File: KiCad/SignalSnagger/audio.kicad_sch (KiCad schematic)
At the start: 56 parts, among them U301 LM386, U302 LT6231, U303 LT6231, U304 LM386

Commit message: Ver 0.24
Schematic updates.
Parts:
- removed SW301: (no value), symbol Switch:SW_SPST
- added C326: 100nF, symbol Device:C_Small
- added C327: 1uF, symbol Device:C_Small
- added D302: CDBA340-HF, Diode_SMD:D_SMA, symbol Diode:CDBA340-HF
- added J302, J303, J304: 36-5006-ND, symbol Connector_Generic:Conn_01x01
- added JP301: (no value), symbol Jumper:SolderJumper_2_Open
- added R323: (no value), symbol Device:R_US
- added R324: 330k, symbol Device:R_US
- added R325: 10k, symbol Device:R_US
- added R326: 1k, symbol Device:R_US
- added R327: 51k, symbol Device:R_US
- J301: value (none) -> Headphones
- R316: value (none) -> 470
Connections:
- net +5V: now also R324.1
- net GND: now also C327.1, J304.1 (Pin_1), R325.2, R327.2
- net Headphone: now also C326.1, JP301.1 (A)
- net I OUT: now also J303.1 (Pin_1)
- net Q OUT: now also J302.1 (Pin_1)
- net at C308.1: now also R323.1
- net at J301.S: now also JP301.2 (B), R323.2
- new net: D302.1 (K), R326.1
- new net: C326.2, D302.2 (A), R324.2, R325.1
- new net ASSI_FAR: C327.2, R326.2, R327.1
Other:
- note removed: "How to protect U301 in the event that someone uses a mono headphone plug?"
- moved on the sheet: C301, C302, C303, C304, C305, C306, C307, C308, C309, C310, C311, C312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

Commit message: V0.25
Schematic updates
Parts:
- removed C312, C317: 100nF, symbol Device:C_Small
- JP301: value (none) -> SolderJumper_2_Open
- R323: value (none) -> 10
- U302, U303: value LT6231 -> TS912IDT; footprint Package_TO_SOT_SMD:TSOT-23-6 -> Package_SO:SO-8_3.9x4.9mm_P1.27mm
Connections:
- net +5V: no longer U302.8 (V+), U303.8 (V+)
- net GND: no longer U302.4 (V-), U303.4 (V-)
- net VG: now also U302.5 (+), U303.5 (+); no longer U302.3 (+), U303.3 (+)
- net at C316.1, C318.2, R319.2: now also U303.7 (OUT); no longer U303.1 (OUT)
- net at C315.1, R319.1: now also U303.6 (-); no longer U303.2 (-)
- net at C310.1, R306.1: now also U302.6 (-); no longer U302.2 (-)
- net at C309.1, C311.1, C313.1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: now also U302.7 (OUT); no longer U302.1 (OUT)
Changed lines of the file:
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@@
   (title_block
     (title "SignalSnagger")
-    (date "2024-02-03")
-    (rev "0.24")
+    (date "2024-02-09")
+    (rev "0.25")
   )
   (junction (at 30.48 160.02) (diameter 0) (color 0 0 0 0)
@@
   (junction (at 196.85 46.99) (diameter 0) (color 0 0 0 0)
   )
-  (junction (at 85.09 48.26) (diameter 0) (color 0 0 0 0)
-  )
   (junction (at 97.79 57.15) (diameter 0) (color 0 0 0 0)
   )
@@
   )
   (junction (at 106.68 151.13) (diameter 0) (color 0 0 0 0)
-  )
-  (junction (at 85.09 142.24) (diameter 0) (color 0 0 0 0)
   )
   (junction (at 238.76 127) (diameter 0) (color 0 0 0 0)
@@
     (stroke (width 0) (type default) (color 0 0 0 0))
   )
-  (wire (pts (xy 86.36 48.26) (xy 85.09 48.26))
-    (stroke (width 0) (type default) (color 0 0 0 0))
-  )
   (wire (pts (xy 72.39 54.61) (xy 76.2 54.61))
     (stroke (width 0) (type default) (color 0 0 0 0))
@@
     (stroke (width 0) (type default) (color 0 0 0 0))
   )
-  (wire (pts (xy 85.09 48.26) (xy 85.09 49.53))
-    (stroke (width 0) (type default) (color 0 0 0 0))
-  )
   (wire (pts (xy 196.85 69.85) (xy 196.85 67.31))
     (stroke (width 0) (type default) (color 0 0 0 0))
@@
     (stroke (width 0) (type default) (color 0 0 0 0))
   )
-  (wire (pts (xy 86.36 142.24) (xy 85.09 142.24))
-    (stroke (width 0) (type default) (color 0 0 0 0))
-  )
   (wire (pts (xy 196.85 107.95) (xy 199.39 107.95))
     (stroke (width 0) (type default) (color 0 0 0 0))
@@
   )
   (wire (pts (xy 124.46 152.4) (xy 124.46 151.13))
-    (stroke (width 0) (type default) (color 0 0 0 0))
-  )
-  (wire (pts (xy 85.09 142.24) (xy 85.09 143.51))
     (stroke (width 0) (type default) (color 0 0 0 0))
   )
@@
       (effects (font (size 1.27 1.27)) (justify left))
     )
-    (property "Value" "" (id 1) (at 227.711 79.1722 0)
+    (property "Value" "10" (id 1) (at 227.711 79.1722 0)
       (effects (font (size 1.27 1.27)) (justify left))
     )
@@
     (pin "3")
   )
-  (symbol (lib_id "Amplifier_Operational:LT6231") (at 87.63 57.15 0) (mirror x) (unit 1)
+  (symbol (lib_id "Amplifier_Operational:LT6231") (at 87.63 57.15 0) (mirror x) (unit 2)
     (in_bom yes) (on_board yes)
     (property "Reference" "U303" (id 0) (at 87.63 53.34 0)
       (effects (font (size 1.524 1.524) bold) (justify left))
     )
-    (property "Value" "LT6231" (id 1) (at 82.55 57.15 0)
-      (effects (font (size 1.27 1.27)) (justify left))
-    )
-    (property "Footprint" "Package_TO_SOT_SMD:TSOT-23-6" (id 2) (at 87.63 50.8 0)
+    (property "Value" "TS912IDT" (id 1) (at 82.55 57.15 0)
+      (effects (font (size 1.27 1.27)) (justify left))
+    )
+    (property "Footprint" "Package_SO:SO-8_3.9x4.9mm_P1.27mm" (id 2) (at 87.63 50.8 0)
       (effects (font (size 1.27 1.27)) hide)
     )
@@
     (pin "1")
   )
-  (symbol (lib_id "power:+5V") (at 85.09 48.26 0) (unit 1)
-    (in_bom yes) (on_board yes) (fields_autoplaced)
-    (property "Reference" "#PWR0309" (id 0) (at 85.09 52.07 0)
-      (effects (font (size 1.27 1.27)) hide)
-    )
-    (property "Value" "+5V" (id 1) (at 85.09 44.6842 0))
-    (property "Footprint" "" (id 2) (at 85.09 48.26 0)
-      (effects (font (size 1.27 1.27)) hide)
-    )
-    (property "Datasheet" "" (id 3) (at 85.09 48.26 0)
-      (effects (font (size 1.27 1.27)) hide)
-    )
-    (pin "1")
-  )
   (symbol (lib_id "Device:R_US") (at 62.23 63.5 0) (unit 1)
     (in_bom yes) (on_board yes)
@@
     (pin "2")
   )
-  (symbol (lib_id "Device:C_Small") (at 88.9 142.24 90) (unit 1)
-    (in_bom yes) (on_board yes)
-    (property "Reference" "C312" (id 0) (at 88.9 139.7 90))
-    (property "Value" "100nF" (id 1) (at 88.9 144.78 90))
-    (property "Footprint" "" (id 2) (at 88.9 142.24 0)
-      (effects (font (size 1.27 1.27)) hide)
-    )
-    (property "Datasheet" "~" (id 3) (at 88.9 142.24 0)
-      (effects (font (size 1.27 1.27)) hide)
-    )
-    (pin "1")
-    (pin "2")
-  )
   (symbol (lib_id "Connector_Generic:Conn_01x01") (at 30.48 124.46 90) (unit 1)
     (in_bom yes) (on_board yes)
@@
     (pin "2")
   )
-  (symbol (lib_id "power:GND") (at 85.09 158.75 0) (unit 1)
-    (in_bom yes) (on_board yes) (fields_autoplaced)
-    (property "Reference" "#PWR0313" (id 0) (at 85.09 165.1 0)
-      (effects (font (size 1.27 1.27)) hide)
-    )
-    (property "Value" "GND" (id 1) (at 85.09 163.1934 0))
-    (property "Footprint" "" (id 2) (at 85.09 158.75 0)
-      (effects (font (size 1.27 1.27)) hide)
-    )
-    (property "Datasheet" "" (id 3) (at 85.09 158.75 0)
-      (effects (font (size 1.27 1.27)) hide)
-    )
-    (pin "1")
-  )
   (symbol (lib_id "Device:C_Small") (at 69.85 148.59 270) (unit 1)
     (in_bom yes) (on_board yes)
@@
     )
     (property "Datasheet" "~" (id 3) (at 69.85 148.59 0)
-      (effects (font (size 1.27 1.27)) hide)
-    )
-    (pin "1")
-    (pin "2")
-  )
-  (symbol (lib_id "Device:C_Small") (at 88.9 48.26 90) (unit 1)
-    (in_bom yes) (on_board yes)
-    (property "Reference" "C317" (id 0) (at 88.9 45.72 90))
-    (property "Value" "100nF" (id 1) (at 88.9 50.8 90))
-    (property "Footprint" "" (id 2) (at 88.9 48.26 0)
-      (effects (font (size 1.27 1.27)) hide)
-    )
-    (property "Datasheet" "~" (id 3) (at 88.9 48.26 0)
       (effects (font (size 1.27 1.27)) hide)
     )
@@
     (pin "1")
   )
-  (symbol (lib_id "power:GND") (at 91.44 48.26 90) (mirror x) (unit 1)
-    (in_bom yes) (on_board yes) (fields_autoplaced)
-    (property "Reference" "#PWR0321" (id 0) (at 97.79 48.26 0)
-      (effects (font (size 1.27 1.27)) hide)
-    )
-    (property "Value" "GND" (id 1) (at 94.615 48.6938 90)
-      (effects (font (size 1.27 1.27)) (justify right) hide)
-    )
-    (property "Footprint" "" (id 2) (at 91.44 48.26 0)
-      (effects (font (size 1.27 1.27)) hide)
-    )
-    (property "Datasheet" "" (id 3) (at 91.44 48.26 0)
-      (effects (font (size 1.27 1.27)) hide)
-    )
-    (pin "1")
-  )
   (symbol (lib_id "Jumper:SolderJumper_2_Open") (at 220.98 100.33 90) (unit 1)
     (in_bom yes) (on_board yes)
@@
       (effects (font (size 1.27 1.27)) (justify right))
     )
-    (property "Value" "" (id 1) (at 222.631 102.0322 90)
+    (property "Value" "SolderJumper_2_Open" (id 1) (at 222.631 102.0322 90)
       (effects (font (size 1.27 1.27)) (justify right) hide)
     )
@@
     (pin "2")
   )
-  (symbol (lib_id "power:GND") (at 85.09 64.77 0) (unit 1)
-    (in_bom yes) (on_board yes) (fields_autoplaced)
-    (property "Reference" "#PWR0320" (id 0) (at 85.09 71.12 0)
-      (effects (font (size 1.27 1.27)) hide)
-    )
-    (property "Value" "GND" (id 1) (at 85.09 69.2134 0))
-    (property "Footprint" "" (id 2) (at 85.09 64.77 0)
-      (effects (font (size 1.27 1.27)) hide)
-    )
-    (property "Datasheet" "" (id 3) (at 85.09 64.77 0)
-      (effects (font (size 1.27 1.27)) hide)
-    )
-    (pin "1")
-  )
-  (symbol (lib_id "Amplifier_Operational:LT6231") (at 87.63 151.13 0) (mirror x) (unit 1)
+  (symbol (lib_id "Amplifier_Operational:LT6231") (at 87.63 151.13 0) (mirror x) (unit 2)
     (in_bom yes) (on_board yes)
     (property "Reference" "U302" (id 0) (at 87.63 147.32 0)
       (effects (font (size 1.524 1.524) bold) (justify left))
     )
-    (property "Value" "LT6231" (id 1) (at 82.55 151.13 0)
-      (effects (font (size 1.27 1.27)) (justify left))
-    )
-    (property "Footprint" "Package_TO_SOT_SMD:TSOT-23-6" (id 2) (at 87.63 144.78 0)
+    (property "Value" "TS912IDT" (id 1) (at 82.55 151.13 0)
+      (effects (font (size 1.27 1.27)) (justify left))
+    )
+    (property "Footprint" "Package_SO:SO-8_3.9x4.9mm_P1.27mm" (id 2) (at 87.63 144.78 0)
       (effects (font (size 1.27 1.27)) hide)
     )
@@
     (pin "2")
   )
-  (symbol (lib_id "power:+5V") (at 85.09 142.24 0) (unit 1)
-    (in_bom yes) (on_board yes) (fields_autoplaced)
-    (property "Reference" "#PWR0312" (id 0) (at 85.09 146.05 0)
-      (effects (font (size 1.27 1.27)) hide)
-    )
-    (property "Value" "+5V" (id 1) (at 85.09 138.6642 0))
-    (property "Footprint" "" (id 2) (at 85.09 142.24 0)
-      (effects (font (size 1.27 1.27)) hide)
-    )
-    (property "Datasheet" "" (id 3) (at 85.09 142.24 0)
-      (effects (font (size 1.27 1.27)) hide)
-    )
-    (pin "1")
-  )
   (symbol (lib_id "Device:C_Small") (at 201.93 139.7 180) (unit 1)
     (in_bom yes) (on_board yes) (fields_autoplaced)
@@
     (pin "2")
   )
-  (symbol (lib_id "power:GND") (at 91.44 142.24 90) (mirror x) (unit 1)
-    (in_bom yes) (on_board yes) (fields_autoplaced)
-    (property "Reference" "#PWR0314" (id 0) (at 97.79 142.24 0)
-      (effects (font (size 1.27 1.27)) hide)
-    )
-    (property "Value" "GND" (id 1) (at 94.615 142.6738 90)
-      (effects (font (size 1.27 1.27)) (justify right) hide)
-    )
-    (property "Footprint" "" (id 2) (at 91.44 142.24 0)
-      (effects (font (size 1.27 1.27)) hide)
-    )
-    (property "Datasheet" "" (id 3) (at 91.44 142.24 0)
-      (effects (font (size 1.27 1.27)) hide)
-    )
-    (pin "1")
-  )
   (symbol (lib_id "Device:R_US") (at 86.36 39.37 90) (unit 1)

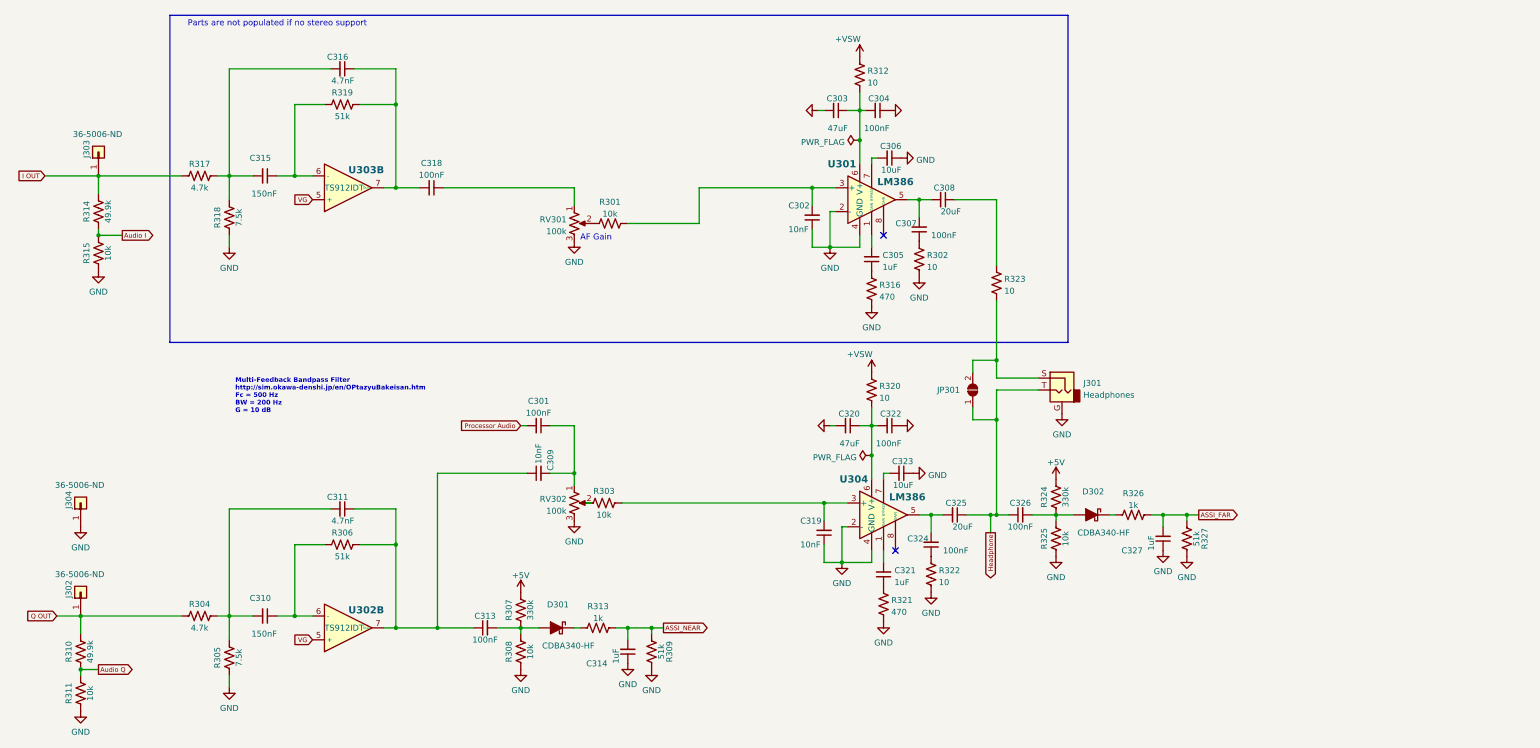
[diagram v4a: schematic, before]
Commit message: Rev 0.28
Adding footprints to schematic: ~10% done
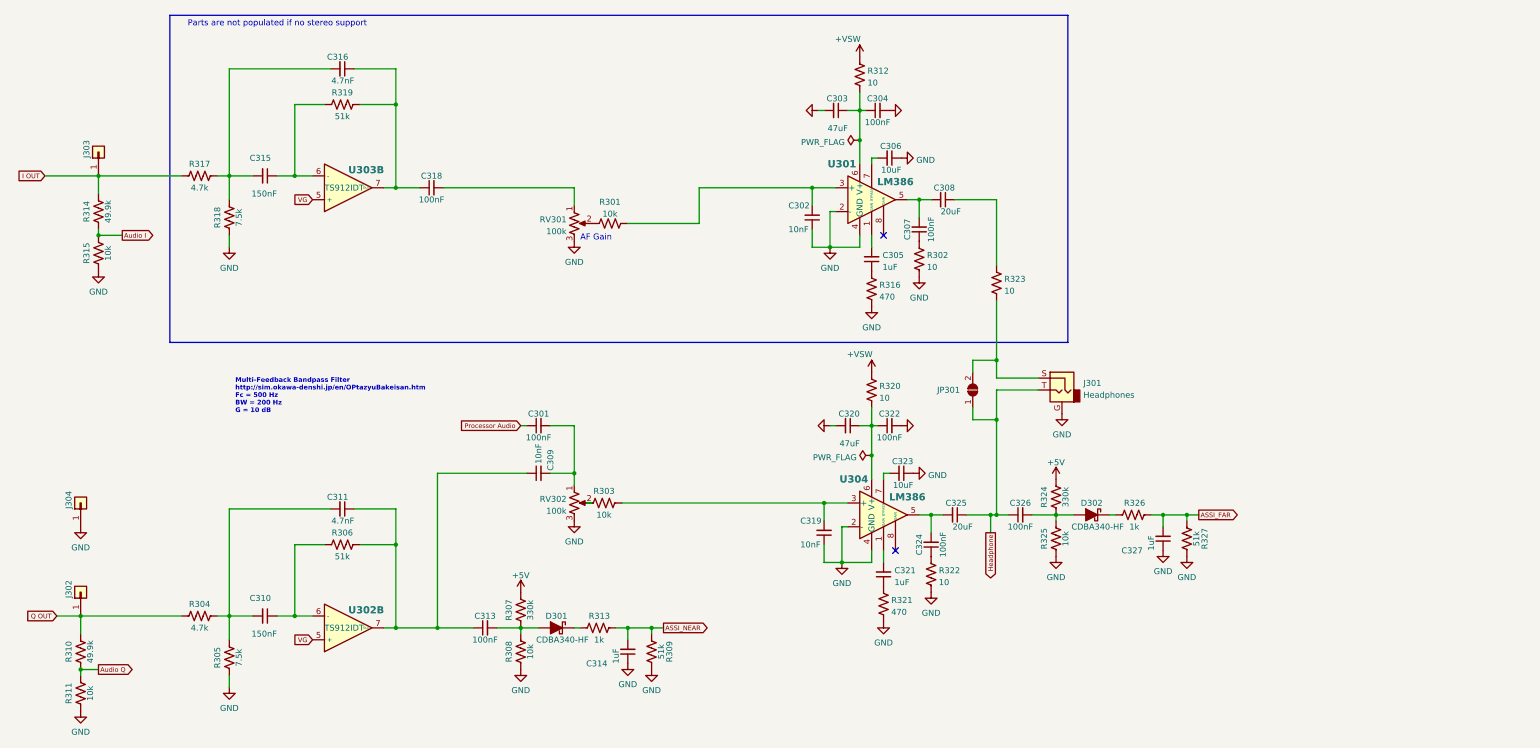
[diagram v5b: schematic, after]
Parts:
- C301, C304, C307, C313, C318, C322, C324, C326: footprint (none) -> Capacitor_SMD:C_0603_1608Metric; Digi-Key Part No. (none) -> 1276-1006-1-ND; Link (none) -> https://www.digikey.com/en/products/detail/samsung-electro-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; Manufacturer (none) -> Samsung Electro-Mechanics; Manufacturer PN (none) -> CL10B104KA8NNNC
- J302, J303, J304: value 36-5006-ND -> (none)
- R313, R326: footprint (none) -> Resistor_SMD:R_0603_1608Metric; Digi-Key Part No. (none) -> 311-1.00KHRCT-ND; Link (none) -> https://www.digikey.com/en/products/detail/yageo/RC0603FR-0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; Manufacturer (none) -> YAGEO; Manufacturer PN (none) -> RC0603FR-071KL
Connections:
- net GND: now also C304.2, C322.2; no longer C304.1, C322.1
- net Processor Audio: now also C301.1; no longer C301.2
- net at C303.1, R312.2, U301.6 (V+): now also C304.1; no longer C304.2
- net at RV301.1: now also C318.2; no longer C318.1
- net at C316.1, R319.2, U303.7 (OUT): now also C318.1; no longer C318.2
- net at C320.1, R320.2, U304.6 (V+): now also C322.1; no longer C322.2
- net at C309.2, RV302.1: now also C301.2; no longer C301.1

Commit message: Ver 0.29
Schematic updates
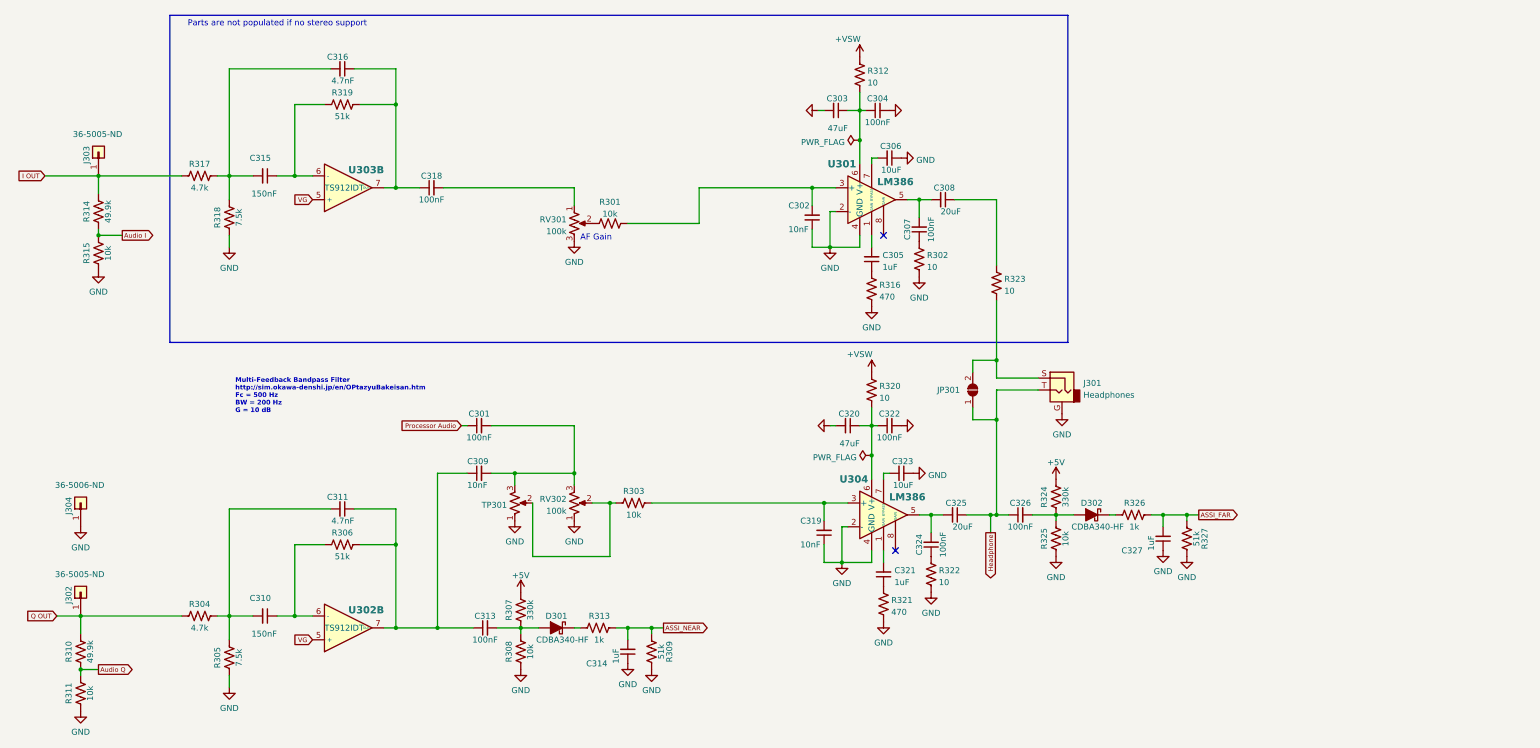
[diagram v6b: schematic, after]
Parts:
- added TP301: (no value), symbol Device:R_Potentiometer_US
- J302, J303: value (none) -> 36-5005-ND; footprint (none) -> Connector_Pin:Pin_D1.6mm_L8.5mm_W2.8mm_FlatFork
- J304: value (none) -> 36-5006-ND; footprint (none) -> Connector_Pin:Pin_D1.6mm_L8.5mm_W2.8mm_FlatFork
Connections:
- net GND: now also RV302.1, TP301.1; no longer RV302.3
- net at R303.1, RV302.2: now also TP301.2
- net at C301.2, C309.2: now also RV302.3, TP301.3; no longer RV302.1
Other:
- moved on the sheet: C301, C309, R303

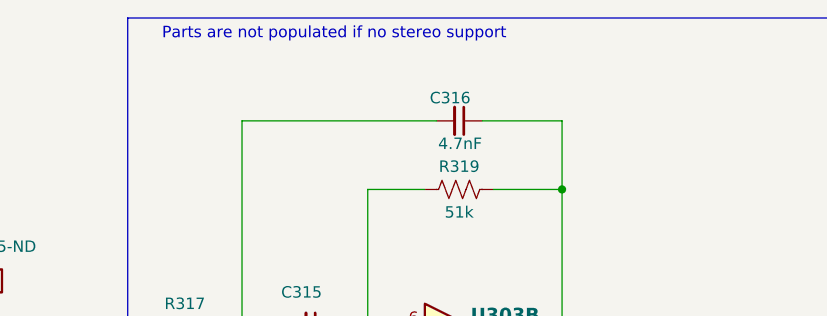
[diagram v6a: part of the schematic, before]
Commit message: Minor Cleanup
No functional changes, only cosmetic changes to the schematic
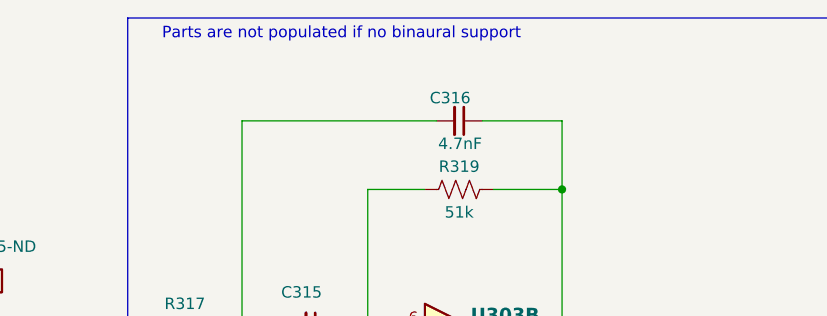
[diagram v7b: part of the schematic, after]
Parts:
- TP301: value (none) -> 100k; footprint (none) -> Connector_PinHeader_2.54mm:PinHeader_1x03_P2.54mm_Vertical
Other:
- note added: "Parts are not populated if no binaural support"
- note removed: "Parts are not populated if no stereo support"
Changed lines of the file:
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@@
     (stroke (width 0) (type default) (color 0 0 0 0))
   )
-  (text "Parts are not populated if no stereo support" (at 53.34 22.86 0)
+  (text "Parts are not populated if no binaural support" (at 53.34 22.86 0)
     (effects (font (size 1.27 1.27)) (justify left bottom))
   )
@@
       (effects (font (size 1.27 1.27)) (justify right))
     )
-    (property "Value" "" (id 1) (at 121.5391 122.7578 0)
+    (property "Value" "100k" (id 1) (at 121.5391 122.7578 0)
       (effects (font (size 1.27 1.27)) (justify right) hide)
     )
-    (property "Footprint" "" (id 2) (at 123.19 124.46 0)
-      (effects (font (size 1.27 1.27)) hide)
-    )
+    (property "Footprint" "Connector_PinHeader_2.54mm:PinHeader_1x03_P2.54mm_Vertical" (id 2) (at 123.19 124.46 0)
+      (effects (font (size 1.27 1.27)) hide)
+    )
